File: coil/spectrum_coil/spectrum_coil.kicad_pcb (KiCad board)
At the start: 2 copper layers, 11 x 11 mm, 1 part, among them T1 Coil

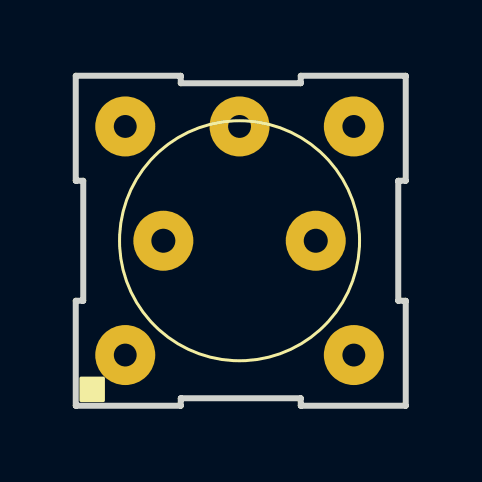
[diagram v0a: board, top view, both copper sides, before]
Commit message: created ibom
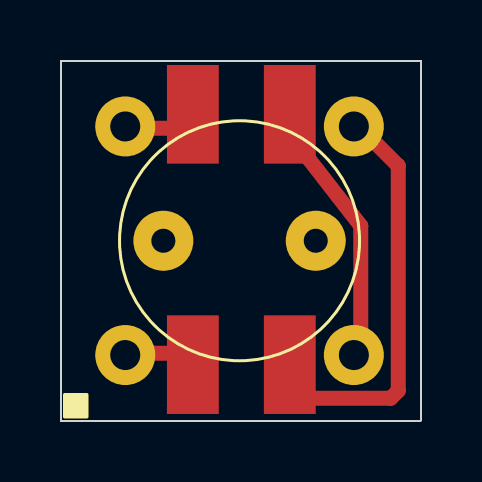
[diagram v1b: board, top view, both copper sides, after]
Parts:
- added REF**: MSD1278-103MLD_COC, coil:MSD1278-103MLD_COC, F.Cu at (121.2, 60.8)
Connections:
- T1 pad 2: unconnected-(T1-AB-Pad2) -> (no net)
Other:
- board size 11 x 11 mm -> 12 x 12 mm
